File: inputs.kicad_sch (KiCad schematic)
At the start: 36 parts, among them J10 Screw_Terminal_01x02, J9 Inputs, Q103 TLP521-4XSM, Q104 TLP521-4XSM

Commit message: First traces added
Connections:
- net D3 is gone; now on net D6: Q103.14 (C_3), R51.2
- net D6: no longer Q104.16 (C_4), R54.2
- net D2 renamed D12
- net D4 renamed D18
- net D5 renamed D21
- net D7 renamed D22
- net D8 renamed D23
- net D9 renamed D20
- new net D19: Q104.16 (C_4), R54.2
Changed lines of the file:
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@@
 		)
 	)
-	(hierarchical_label "D5"
-		(shape bidirectional)
+	(global_label "D23"
+		(shape output)
+		(at 214.63 119.38 0)
+		(fields_autoplaced yes)
+		(effects
+			(font
+				(size 1.27 1.27)
+			)
+			(justify left)
+		)
+		(property "Intersheetrefs" "${INTERSHEET_REFS}"
+			(at 221.3042 119.38 0)
+			(effects
+				(font
+					(size 1.27 1.27)
+				)
+				(justify left)
+				(hide yes)
+			)
+		)
+	)
+	(global_label "D22"
+		(shape output)
+		(at 214.63 114.3 0)
+		(fields_autoplaced yes)
+		(effects
+			(font
+				(size 1.27 1.27)
+			)
+			(justify left)
+		)
+		(property "Intersheetrefs" "${INTERSHEET_REFS}"
+			(at 221.3042 114.3 0)
+			(effects
+				(font
+					(size 1.27 1.27)
+				)
+				(justify left)
+				(hide yes)
+			)
+		)
+	)
+	(global_label "D6"
+		(shape output)
+		(at 214.63 82.55 0)
+		(fields_autoplaced yes)
+		(effects
+			(font
+				(size 1.27 1.27)
+			)
+			(justify left)
+		)
+		(property "Intersheetrefs" "${INTERSHEET_REFS}"
+			(at 220.0947 82.55 0)
+			(effects
+				(font
+					(size 1.27 1.27)
+				)
+				(justify left)
+				(hide yes)
+			)
+		)
+	)
+	(global_label "D19"
+		(shape output)
+		(at 214.63 109.22 0)
+		(fields_autoplaced yes)
+		(effects
+			(font
+				(size 1.27 1.27)
+			)
+			(justify left)
+		)
+		(property "Intersheetrefs" "${INTERSHEET_REFS}"
+			(at 221.3042 109.22 0)
+			(effects
+				(font
+					(size 1.27 1.27)
+				)
+				(justify left)
+				(hide yes)
+			)
+		)
+	)
+	(global_label "D12"
+		(shape output)
+		(at 214.63 77.47 0)
+		(fields_autoplaced yes)
+		(effects
+			(font
+				(size 1.27 1.27)
+			)
+			(justify left)
+		)
+		(property "Intersheetrefs" "${INTERSHEET_REFS}"
+			(at 221.3042 77.47 0)
+			(effects
+				(font
+					(size 1.27 1.27)
+				)
+				(justify left)
+				(hide yes)
+			)
+		)
+	)
+	(global_label "D18"
+		(shape output)
+		(at 214.63 87.63 0)
+		(fields_autoplaced yes)
+		(effects
+			(font
+				(size 1.27 1.27)
+			)
+			(justify left)
+		)
+		(property "Intersheetrefs" "${INTERSHEET_REFS}"
+			(at 221.3042 87.63 0)
+			(effects
+				(font
+					(size 1.27 1.27)
+				)
+				(justify left)
+				(hide yes)
+			)
+		)
+	)
+	(global_label "D20"
+		(shape output)
+		(at 214.63 124.46 0)
+		(fields_autoplaced yes)
+		(effects
+			(font
+				(size 1.27 1.27)
+			)
+			(justify left)
+		)
+		(property "Intersheetrefs" "${INTERSHEET_REFS}"
+			(at 221.3042 124.46 0)
+			(effects
+				(font
+					(size 1.27 1.27)
+				)
+				(justify left)
+				(hide yes)
+			)
+		)
+	)
+	(global_label "D21"
+		(shape output)
 		(at 214.63 92.71 0)
 		(fields_autoplaced yes)
@@
 			(justify left)
 		)
-	)
-	(hierarchical_label "D7"
-		(shape bidirectional)
-		(at 214.63 114.3 0)
-		(fields_autoplaced yes)
-		(effects
-			(font
-				(size 1.27 1.27)
+		(property "Intersheetrefs" "${INTERSHEET_REFS}"
+			(at 221.3042 92.71 0)
+			(effects
+				(font
+					(size 1.27 1.27)
+				)
+				(justify left)
+				(hide yes)
 			)
-			(justify left)
 		)
 	)
-	(hierarchical_label "D3"
-		(shape bidirectional)
-		(at 214.63 82.55 0)
-		(fields_autoplaced yes)
-		(effects
-			(font
-				(size 1.27 1.27)
-			)
-			(justify left)
-		)
-	)
-	(hierarchical_label "D6"
-		(shape bidirectional)
-		(at 214.63 109.22 0)
-		(fields_autoplaced yes)
-		(effects
-			(font
-				(size 1.27 1.27)
-			)
-			(justify left)
-		)
-	)
-	(hierarchical_label "D8"
-		(shape bidirectional)
-		(at 214.63 119.38 0)
-		(fields_autoplaced yes)
-		(effects
-			(font
-				(size 1.27 1.27)
-			)
-			(justify left)
-		)
-	)
-	(hierarchical_label "D9"
-		(shape bidirectional)
-		(at 214.63 124.46 0)
-		(fields_autoplaced yes)
-		(effects
-			(font
-				(size 1.27 1.27)
-			)
-			(justify left)
-		)
-	)
-	(hierarchical_label "D4"
-		(shape bidirectional)
-		(at 214.63 87.63 0)
-		(fields_autoplaced yes)
-		(effects
-			(font
-				(size 1.27 1.27)
-			)
-			(justify left)
-		)
-	)
-	(hierarchical_label "D2"
-		(shape bidirectional)
-		(at 214.63 77.47 0)
-		(fields_autoplaced yes)
-		(effects
-			(font
-				(size 1.27 1.27)
-			)
-			(justify left)
-		)
-	)

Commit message: More traces + components alignment
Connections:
- net at D19.1 (K): now also Q103.5 (A_3); no longer Q103.3 (A_2)
- net at Q103.1 (A_1): now also D21.1 (K); no longer D18.1 (K)
- net at J9.8 (Pin_8), R34.2: now also Q103.8 (K_4); no longer Q103.2 (K_1)
- net at J9.7 (Pin_7), R35.2: now also Q103.6 (K_3); no longer Q103.4 (K_2)
- net at D20.1 (K): now also Q103.3 (A_2); no longer Q103.5 (A_3)
- net at J9.6 (Pin_6), R36.2: now also Q103.4 (K_2); no longer Q103.6 (K_3)
- net at Q103.7 (A_4): now also D18.1 (K); no longer D21.1 (K)
- net at J9.5 (Pin_5), R37.2: now also Q103.2 (K_1); no longer Q103.8 (K_4)
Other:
- moved on the sheet: D18, D19, D20, D21, R42, R43, R44, R45, R50, R51, R52, R53

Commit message: Made the PCK the size of the LP board
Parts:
- removed Q103, Q104: TLP521-4XSM, SamacSys_Parts:TLP5214XSM, symbol SamacSys_Parts:TLP521-4XSM
- added U4, U5: TCMT4100, Package_SO:SOP-16_4.4x10.4mm_P1.27mm, symbol Isolator:TCMT4100
- R34: value 10k -> -> 10k
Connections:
- net D12: now also U4.16
- net D18: now also U4.12
- net D19: now also U5.16
- net D20: now also U5.10
- net D21: now also U4.10
- net D22: now also U5.14
- net D23: now also U5.12
- net D6: now also U4.14
- net GND: now also U4.11, U4.13, U4.15, U4.9, U5.11, U5.13, U5.15, U5.9
- net at D23.1 (K): now also U5.3
- net at D19.1 (K): now also U4.5
- net at D21.1 (K): now also U4.1
- net at J9.5 (Pin_5), R37.2: now also U4.2
- net at D20.1 (K): now also U4.3
- net at J9.6 (Pin_6), R36.2: now also U4.4
- net at J9.7 (Pin_7), R35.2: now also U4.6
- net at D18.1 (K): now also U4.7
- net at J9.8 (Pin_8), R34.2: now also U4.8
- net at D22.1 (K): now also U5.1
- net at D24.1 (K): now also U5.5
- net at J9.1 (Pin_1), R41.2: now also U5.8
- net at J9.2 (Pin_2), R40.2: now also U5.6
- net at J9.3 (Pin_3), R39.2: now also U5.4
- net at J9.4 (Pin_4), R38.2: now also U5.2
- net at D25.1 (K): now also U5.7
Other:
- moved on the sheet: D18, D19, D20, D21, D22, D23, D24, D25, J10, J9, R34, R35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

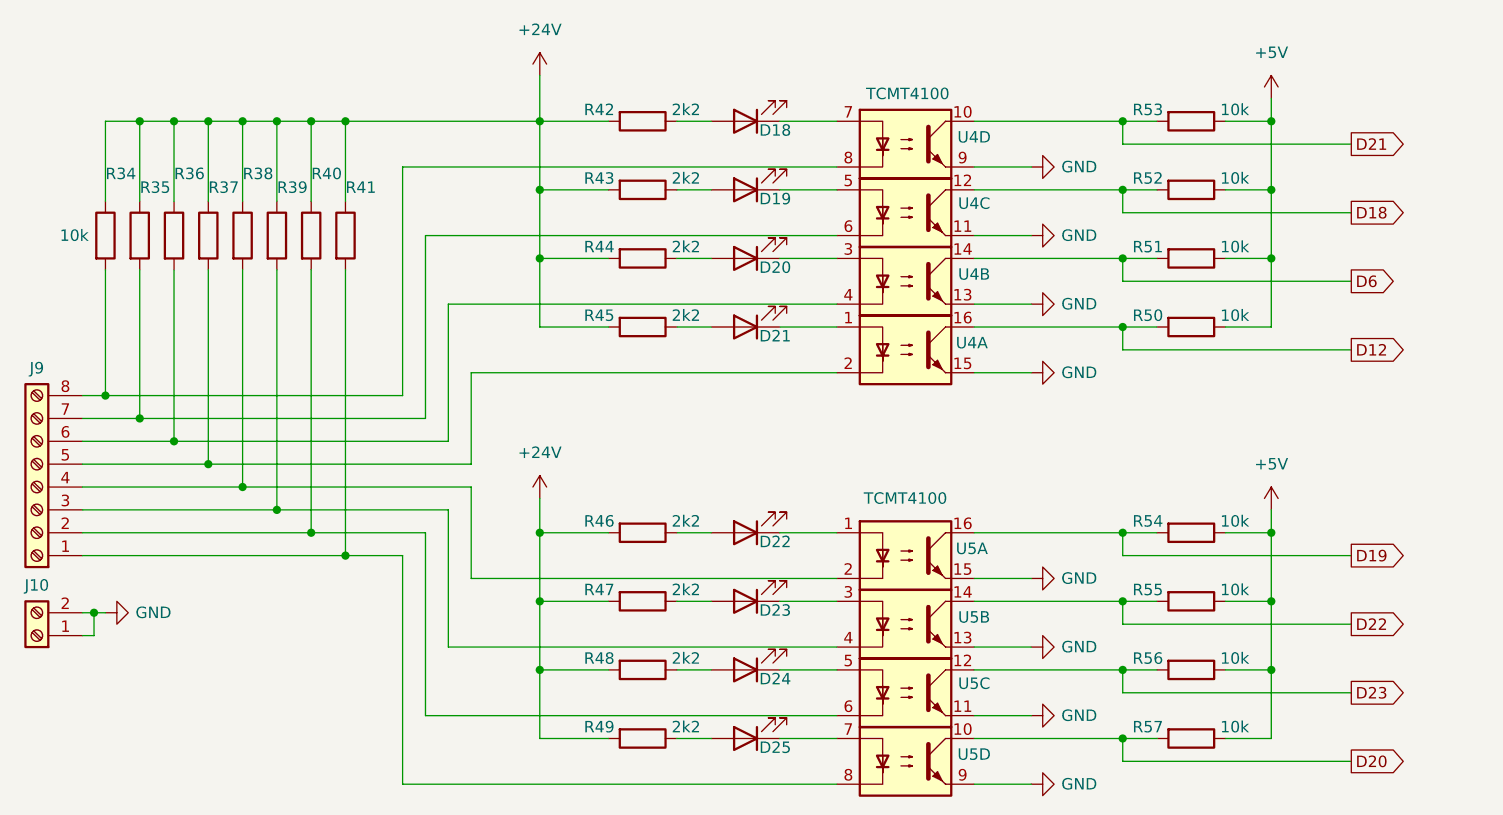
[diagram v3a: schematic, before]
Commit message: PCB shortened to final measurements
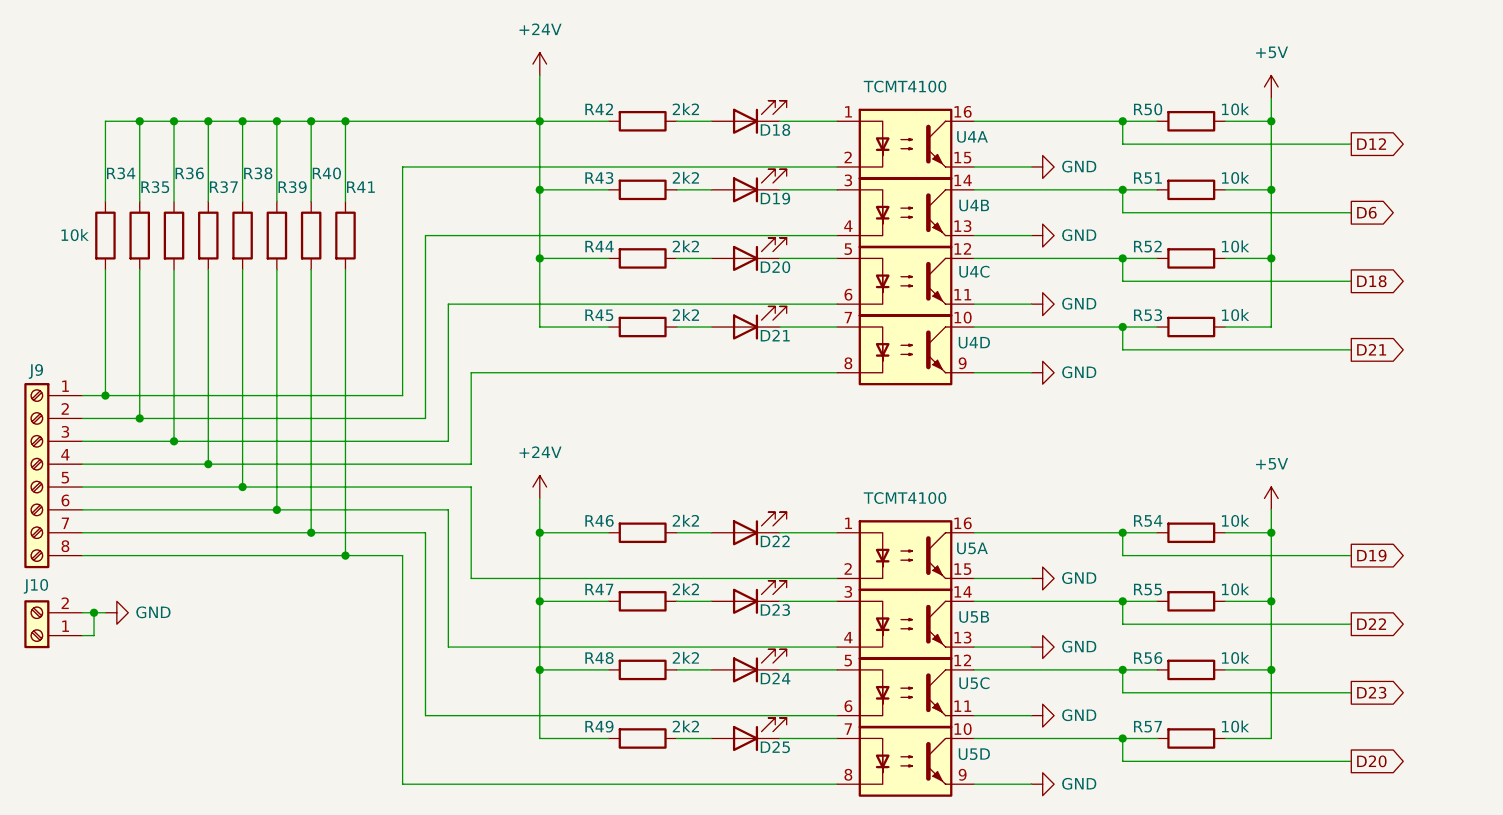
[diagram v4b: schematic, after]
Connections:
- net at D19.1 (K): now also U4.3; no longer U4.5
- net at D18.1 (K): now also U4.1; no longer U4.7
- net at D20.1 (K): now also U4.5; no longer U4.3
- net at R40.2, U5.6: now also J9.7 (Pin_7); no longer J9.2 (Pin_2)
- net at R38.2, U5.2: now also J9.5 (Pin_5); no longer J9.4 (Pin_4)
- net at R41.2, U5.8: now also J9.8 (Pin_8); no longer J9.1 (Pin_1)
- net at R39.2, U5.4: now also J9.6 (Pin_6); no longer J9.3 (Pin_3)
- net at D21.1 (K): now also U4.7; no longer U4.1
- new net: J9.4 (Pin_4), R37.2, U4.8
- new net: J9.2 (Pin_2), R35.2, U4.4
- new net: J9.3 (Pin_3), R36.2, U4.6
- new net: J9.1 (Pin_1), R34.2, U4.2
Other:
- moved on the sheet: J9, R50, R51, R52, R53, U4A, U4B, U4C, U4D
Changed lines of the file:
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@@
 	(global_label "D6"
 		(shape output)
-		(at 207.01 82.55 0)
+		(at 207.01 74.93 0)
 		(fields_autoplaced yes)
 		(effects
@@
 		)
 		(property "Intersheetrefs" "${INTERSHEET_REFS}"
-			(at 212.4747 82.55 0)
+			(at 212.4747 74.93 0)
 			(effects
 				(font
@@
 	(global_label "D12"
 		(shape output)
-		(at 207.01 90.17 0)
+		(at 207.01 67.31 0)
 		(fields_autoplaced yes)
 		(effects
@@
 		)
 		(property "Intersheetrefs" "${INTERSHEET_REFS}"
-			(at 213.6842 90.17 0)
+			(at 213.6842 67.31 0)
 			(effects
 				(font
@@
 	(global_label "D18"
 		(shape output)
-		(at 207.01 74.93 0)
+		(at 207.01 82.55 0)
 		(fields_autoplaced yes)
 		(effects
@@
 		)
 		(property "Intersheetrefs" "${INTERSHEET_REFS}"
-			(at 213.6842 74.93 0)
+			(at 213.6842 82.55 0)
 			(effects
 				(font
@@
 	(global_label "D21"
 		(shape output)
-		(at 207.01 67.31 0)
+		(at 207.01 90.17 0)
 		(fields_autoplaced yes)
 		(effects
@@
 		)
 		(property "Intersheetrefs" "${INTERSHEET_REFS}"
-			(at 213.6842 67.31 0)
+			(at 213.6842 90.17 0)
 			(effects
 				(font
@@
 	(symbol
 		(lib_id "Device:R")
-		(at 189.23 64.77 270)
+		(at 189.23 87.63 270)
 		(unit 1)
 		(exclude_from_sim no)
@@
 		(dnp no)
 		(property "Reference" "R53"
-			(at 184.404 63.5 90)
+			(at 184.404 86.36 90)
 			(effects
 				(font
@@
 		)
 		(property "Value" "10k"
-			(at 194.056 63.5 90)
+			(at 194.056 86.36 90)
 			(effects
 				(font
@@
 		)
 		(property "Footprint" "Resistor_SMD:R_0603_1608Metric"
-			(at 189.23 62.992 90)
+			(at 189.23 85.852 90)
 			(effects
 				(font
@@
 		)
 		(property "Datasheet" "~"
-			(at 189.23 64.77 0)
+			(at 189.23 87.63 0)
 			(effects
 				(font
@@
 		)
 		(property "Description" "Resistor"
-			(at 189.23 64.77 0)
+			(at 189.23 87.63 0)
 			(effects
 				(font
@@
 	(symbol
 		(lib_id "Device:R")
-		(at 189.23 80.01 270)
+		(at 189.23 72.39 270)
 		(unit 1)
 		(exclude_from_sim no)
@@
 		(dnp no)
 		(property "Reference" "R51"
-			(at 184.404 78.74 90)
+			(at 184.404 71.12 90)
 			(effects
 				(font
@@
 		)
 		(property "Value" "10k"
-			(at 194.056 78.74 90)
+			(at 194.056 71.12 90)
 			(effects
 				(font
@@
 		)
 		(property "Footprint" "Resistor_SMD:R_0603_1608Metric"
-			(at 189.23 78.232 90)
+			(at 189.23 70.612 90)
 			(effects
 				(font
@@
 		)
 		(property "Datasheet" "~"
-			(at 189.23 80.01 0)
+			(at 189.23 72.39 0)
 			(effects
 				(font
@@
 		)
 		(property "Description" "Resistor"
-			(at 189.23 80.01 0)
+			(at 189.23 72.39 0)
 			(effects
 				(font
@@
 	(symbol
 		(lib_id "Isolator:TCMT4100")
-		(at 157.48 82.55 0)
+		(at 157.48 74.93 0)
 		(unit 2)
 		(exclude_from_sim no)
@@
 		(dnp no)
 		(property "Reference" "U4"
-			(at 165.1 81.788 0)
+			(at 165.1 74.168 0)
 			(effects
 				(font
@@
 		)
 		(property "Value" "TCMT4100"
-			(at 157.48 76.2 0)
+			(at 157.48 68.58 0)
 			(effects
 				(font
@@
 		)
 		(property "Footprint" "Package_SO:SOP-16_4.4x10.4mm_P1.27mm"
-			(at 157.48 90.17 0)
+			(at 157.48 82.55 0)
 			(effects
 				(font
@@
 		)
 		(property "Datasheet" "https://www.vishay.com/docs/84181/tcmt4100.pdf"
-			(at 157.48 83.82 0)
+			(at 157.48 76.2 0)
 			(effects
 				(font
@@
 		)
 		(property "Description" "Quad Optocoupler, Vce 70V, CTR 50-600%, Viso 3750V (RMS), SOP-16"
-			(at 157.48 82.55 0)
+			(at 157.48 74.93 0)
 			(effects
 				(font
@@
 	(symbol
 		(lib_id "Isolator:TCMT4100")
-		(at 157.48 74.93 0)
+		(at 157.48 82.55 0)
 		(unit 3)
 		(exclude_from_sim no)
@@
 		(dnp no)
 		(property "Reference" "U4"
-			(at 165.1 73.914 0)
+			(at 165.1 81.534 0)
 			(effects
 				(font
@@
 		)
 		(property "Value" "TCMT4100"
-			(at 157.48 68.58 0)
+			(at 157.48 76.2 0)
 			(effects
 				(font
@@
 		)
 		(property "Footprint" "Package_SO:SOP-16_4.4x10.4mm_P1.27mm"
-			(at 157.48 82.55 0)
+			(at 157.48 90.17 0)
 			(effects
 				(font
@@
 		)
 		(property "Datasheet" "https://www.vishay.com/docs/84181/tcmt4100.pdf"
-			(at 157.48 76.2 0)
+			(at 157.48 83.82 0)
 			(effects
 				(font
@@
 		)
 		(property "Description" "Quad Optocoupler, Vce 70V, CTR 50-600%, Viso 3750V (RMS), SOP-16"
-			(at 157.48 74.93 0)
+			(at 157.48 82.55 0)
 			(effects
 				(font
@@
 	(symbol
 		(lib_id "Connector:Screw_Terminal_01x08")
-		(at 60.96 105.41 180)
+		(at 60.96 102.87 0)
+		(mirror y)
 		(unit 1)
 		(exclude_from_sim no)
@@
 		(dnp no)
 		(property "Reference" "J9"
-			(at 60.96 92.202 0)
+			(at 60.96 92.456 0)
 			(effects
 				(font
@@
 		)
 		(property "Value" "Inputs"
-			(at 60.96 91.44 0)
+			(at 60.96 116.84 0)
 			(effects
 				(font
@@
 		)
 		(property "Footprint" "TerminalBlock_Phoenix:TerminalBlock_Phoenix_PT-1,5-8-3.5-H_1x08_P3.50mm_Horizontal"
-			(at 60.96 105.41 0)
+			(at 60.96 102.87 0)
 			(effects
 				(font
@@
 		)
 		(property "Datasheet" "~"
-			(at 60.96 105.41 0)
+			(at 60.96 102.87 0)
 			(effects
 				(font
@@
 		)
 		(property "Description" "Generic screw terminal, single row, 01x08, script generated (kicad-library-utils/schlib/autogen/connector/)"
-			(at 60.96 105.41 0)
+			(at 60.96 102.87 0)
 			(effects
 				(font
@@
 	(symbol
 		(lib_id "Isolator:TCMT4100")
-		(at 157.48 90.17 0)
+		(at 157.48 67.31 0)
 		(unit 1)
 		(exclude_from_sim no)
@@
 		(dnp no)
 		(property "Reference" "U4"
-			(at 164.846 89.408 0)
+			(at 164.846 66.548 0)
 			(effects
 				(font
@@
 		)
 		(property "Value" "TCMT4100"
-			(at 157.734 61.722 0)
+			(at 157.48 60.96 0)
 			(effects
 				(font
@@
 		)
 		(property "Footprint" "Package_SO:SOP-16_4.4x10.4mm_P1.27mm"
-			(at 157.48 97.79 0)
+			(at 157.48 74.93 0)
 			(effects
 				(font
@@
 		)
 		(property "Datasheet" "https://www.vishay.com/docs/84181/tcmt4100.pdf"
-			(at 157.48 91.44 0)
+			(at 157.48 68.58 0)
 			(effects
 				(font
@@
 		)
 		(property "Description" "Quad Optocoupler, Vce 70V, CTR 50-600%, Viso 3750V (RMS), SOP-16"
-			(at 157.48 90.17 0)
+			(at 157.48 67.31 0)
 			(effects
 				(font
@@
 	(symbol
 		(lib_id "Device:R")
-		(at 189.23 87.63 270)
+		(at 189.23 64.77 270)
 		(unit 1)
 		(exclude_from_sim no)
@@
 		(dnp no)
 		(property "Reference" "R50"
-			(at 184.404 86.36 90)
+			(at 184.404 63.5 90)
 			(effects
 				(font
@@
 		)
 		(property "Value" "10k"
-			(at 194.056 86.36 90)
+			(at 194.056 63.5 90)
 			(effects
 				(font
@@
 		)
 		(property "Footprint" "Resistor_SMD:R_0603_1608Metric"
-			(at 189.23 85.852 90)
+			(at 189.23 62.992 90)
 			(effects
 				(font
@@
 		)
 		(property "Datasheet" "~"
-			(at 189.23 87.63 0)
+			(at 189.23 64.77 0)
 			(effects
 				(font
@@
 		)
 		(property "Description" "Resistor"
-			(at 189.23 87.63 0)
+			(at 189.23 64.77 0)
 			(effects
 				(font
@@
 	(symbol
 		(lib_id "Isolator:TCMT4100")
-		(at 157.48 67.31 0)
+		(at 157.48 90.17 0)
 		(unit 4)
 		(exclude_from_sim no)
@@
 		(dnp no)
 		(property "Reference" "U4"
-			(at 165.1 66.548 0)
+			(at 165.1 89.408 0)
 			(effects
 				(font
@@
 		)
 		(property "Value" "TCMT4100"
-			(at 157.48 60.96 0)
+			(at 157.48 83.82 0)
 			(effects
 				(font
@@
 		)
 		(property "Footprint" "Package_SO:SOP-16_4.4x10.4mm_P1.27mm"
-			(at 157.48 74.93 0)
+			(at 157.48 97.79 0)
 			(effects
 				(font
@@
 		)
 		(property "Datasheet" "https://www.vishay.com/docs/84181/tcmt4100.pdf"
-			(at 157.48 68.58 0)
+			(at 157.48 91.44 0)
 			(effects
 				(font
@@
 		)
 		(property "Description" "Quad Optocoupler, Vce 70V, CTR 50-600%, Viso 3750V (RMS), SOP-16"
-			(at 157.48 67.31 0)
+			(at 157.48 90.17 0)
 			(effects
 				(font
@@
 	(symbol
 		(lib_id "Device:R")
-		(at 189.23 72.39 270)
+		(at 189.23 80.01 270)
 		(unit 1)
 		(exclude_from_sim no)
@@
 		(dnp no)
 		(property "Reference" "R52"
-			(at 184.404 71.12 90)
+			(at 184.404 78.74 90)
 			(effects
 				(font
@@
 		)
 		(property "Value" "10k"
-			(at 194.056 71.12 90)
+			(at 194.056 78.74 90)
 			(effects
 				(font
@@
 		)
 		(property "Footprint" "Resistor_SMD:R_0603_1608Metric"
-			(at 189.23 70.612 90)
+			(at 189.23 78.232 90)
 			(effects
 				(font
@@
 		)
 		(property "Datasheet" "~"
-			(at 189.23 72.39 0)
+			(at 189.23 80.01 0)
 			(effects
 				(font
@@
 		)
 		(property "Description" "Resistor"
-			(at 189.23 72.39 0)
+			(at 189.23 80.01 0)
 			(effects
 				(font
